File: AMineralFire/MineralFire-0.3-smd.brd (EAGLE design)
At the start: 109.9 x 77 mm, 86 parts, among them IC2 74LS09D, IC3 LM358D, Q1 20MHz, Q2 20MHz, Q3 MMBT3906LT1SMD, Q4 MMBT3906LT1SMD, Q5 MMBT3906LT1SMD, Q6 MMBT3906LT1SMD, Q7 MMBT3906LT1SMD, Q8 MMBT3906LT1SMD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

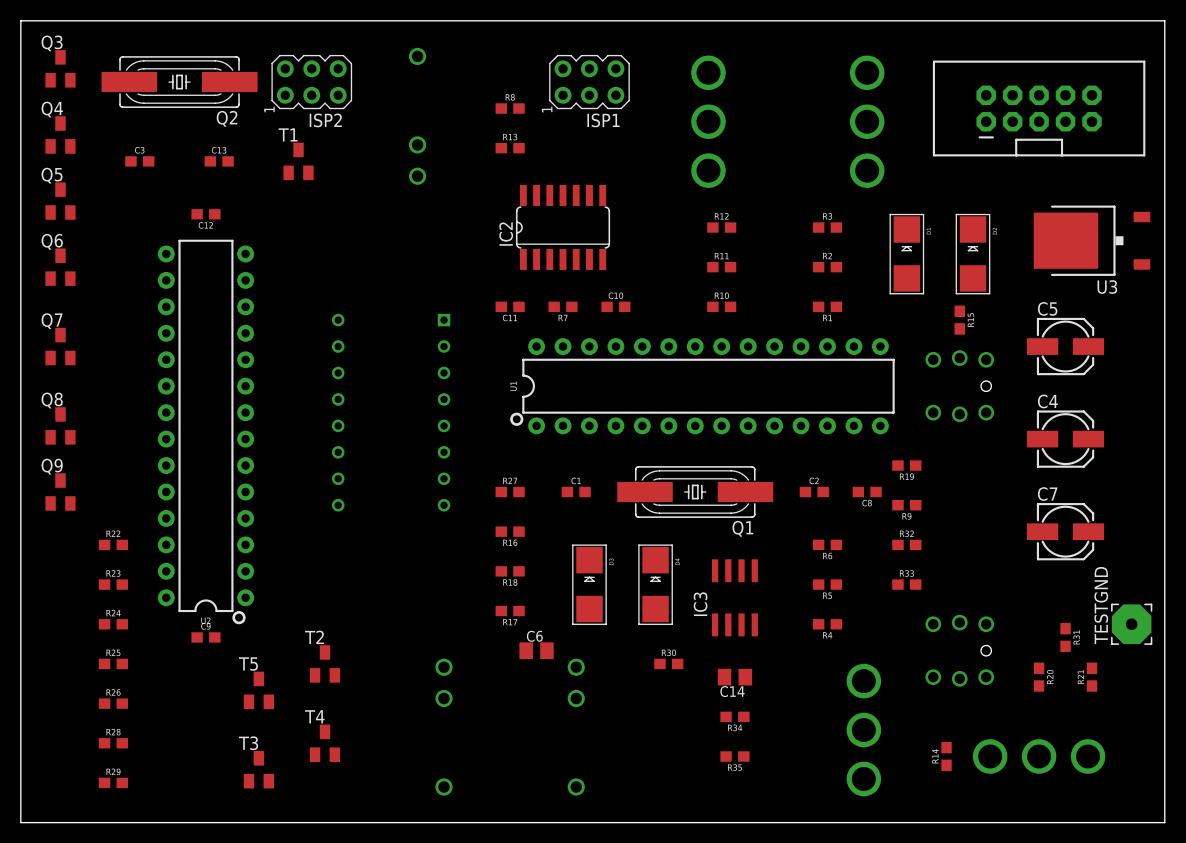
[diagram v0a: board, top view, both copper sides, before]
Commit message: 0.3-smd nor fully smd
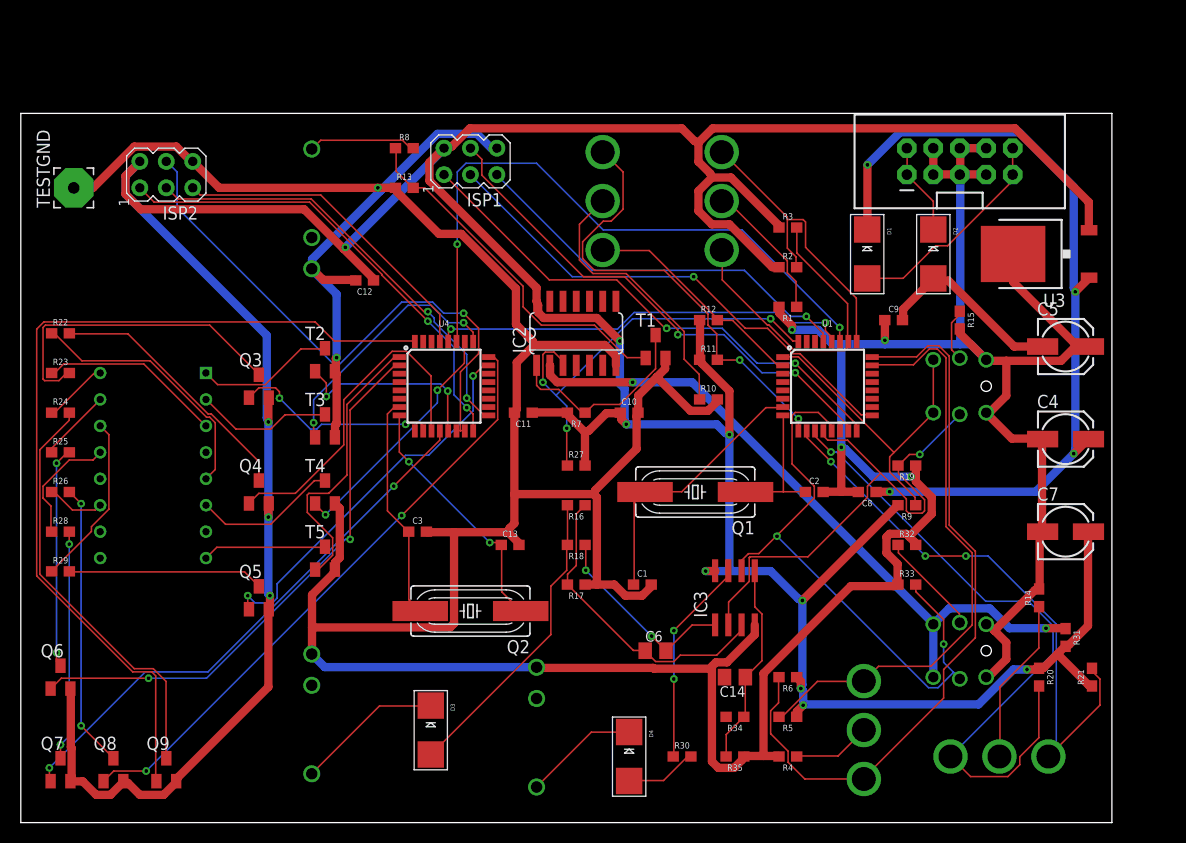
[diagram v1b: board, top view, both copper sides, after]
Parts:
- removed U2: 328P, SparkFun-IC-Microcontroller:DIP28
- added U4: ATMEGA328P_TQFP, SparkFun-IC-Microcontroller:TQFP32-08
- U1: value 328P -> ATMEGA328P_TQFP; device SparkFun-IC-Microcontroller:DIP28 -> SparkFun-IC-Microcontroller:TQFP32-08
- moved TESTGND 109.9 mm to (5.08, 61.0)
- moved C9 72.7 mm to (83.8, 48.3)
- moved Q2 58.0 mm to (43.2, 20.3)
- moved C13 46.2 mm to (47.0, 26.7)
- moved C3 44.5 mm to (38.1, 27.9)
- moved Q5 42.6 mm to (22.9, 21.6)
- moved Q7 40.6 mm to (3.81, 5.08)
- moved Q6 39.4 mm to (3.81, 14.0)
- moved Q4 39.2 mm to (22.9, 31.8)
- moved T1 38.6 mm to (61.0, 45.7)
- moved Q3 35.9 mm to (22.9, 41.9)
- moved T3 33.6 mm to (29.2, 38.1)
- moved Q8 33.4 mm to (8.89, 5.08)
- moved T2 29.2 mm to (29.2, 44.5)
- moved Q9 28.5 mm to (14.0, 5.08)
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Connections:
- net +5V: now also U1.18, U1.4, U4.18, U4.20, U4.4; no longer U1.21, U1.7, U2.20, U2.21, U2.7
- net BUTLED: now also U1.13; no longer U1.15
- net B_TRIG: now also U1.1; no longer U1.5
- net C-DIG1: now also U4.13; no longer U2.15
- net C-DIG2: now also U4.25; no longer U2.25
- net C-DIG3: now also U4.26; no longer U2.26
- net C-DIG4: now also U4.1; no longer U2.5
- net C-SEGA: now also U4.23; no longer U2.23
- net C-SEGB: now also U4.32; no longer U2.4
- net C-SEGC: now also U4.12; no longer U2.14
- net C-SEGD: now also U4.10; no longer U2.12
- net C-SEGDP: now also U4.9; no longer U2.11
- net C-SEGE: now also U4.11; no longer U2.13
- net C-SEGF: now also U4.24; no longer U2.24
- net C-SEGG: now also U4.2; no longer U2.6
- net CS: now also U1.14; no longer U1.16
- net GND: now also U1.3, U1.5, U4.21, U4.3, U4.5; no longer U1.22, U1.8, U2.22, U2.8
- net MISO: now also U1.16; no longer U1.18
- net MISO2: now also U4.16; no longer U2.18
- net MOSI: now also U1.15; no longer U1.17
- net MOSI2: now also U4.14, U4.15; no longer U2.16, U2.17
- net N$1: now also U1.7; no longer U1.9
- net N$2: now also U1.8; no longer U1.10
- net N$7: now also U4.7; no longer U2.9
- net N$8: now also U4.8; no longer U2.10
- net RST: now also U1.29; no longer U1.1
- net RST2: now also U4.29; no longer U2.1
- net SCK: now also U1.17; no longer U1.19
- net SCK2: now also U4.17; no longer U2.19
- net SCL: now also U4.28; no longer U2.28
- net SDA: now also U4.27; no longer U2.27
- net T1: now also U1.9; no longer U1.11
- net T2: now also U1.2; no longer U1.6
- net T7: now also U1.10; no longer U1.12
- net T8: now also U1.11; no longer U1.13
- net TRIG: now also U1.32; no longer U1.4
- net TRIGO: now also U1.12; no longer U1.14
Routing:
- net GND: track 0.00 -> 475.4 mm, vias 0 -> 6
- net +5V: track 0.00 -> 404.2 mm, vias 0 -> 12
- net C-SEGB: track 0.00 -> 86.6 mm
- net +12V: track 0.00 -> 79.6 mm, vias 0 -> 4
- net T6: track 0.00 -> 71.5 mm
- net LBUTTON: track 0.00 -> 66.9 mm, vias 0 -> 2
- net T8: track 0.00 -> 63.8 mm, vias 0 -> 1
- net SDA: track 0.00 -> 61.3 mm, vias 0 -> 2
- net C-SEGF: track 0.00 -> 58.9 mm, vias 0 -> 2
- net BUTLED: track 0.00 -> 58.7 mm, vias 0 -> 2
- net T5: track 0.00 -> 57.1 mm
- net T7: track 0.00 -> 55.9 mm, vias 0 -> 3
- net MOSI2: track 0.00 -> 55.0 mm, vias 0 -> 1
- net C-SEGG: track 0.00 -> 53.6 mm, vias 0 -> 2
- net C-SEGC: track 0.00 -> 52.7 mm, vias 0 -> 2
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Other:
- board size 109.9 x 77 mm -> 104.8 x 68.1 mm

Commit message: Added pull up resistors on I2C comms
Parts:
- added R36, R37: 4k7, SparkFun-Resistors:0603
- moved R10 23.4 mm to (48.3, 55.9)
- moved C1 15.9 mm to (73.7, 30.5)
- moved Q1 14.8 mm to (77.5, 24.1)
- moved C8 12.8 mm to (94.0, 33.0)
- moved R12 7.62 mm to (66.0, 40.6)
- moved IC3 7.41 mm to (62.2, 25.4)
- moved C2 5.24 mm to (81.3, 30.5)
- moved R32 5.24 mm to (90.2, 27.9)
- moved R33 5.24 mm to (90.2, 24.1)
- moved R11 3.81 mm to (66.0, 48.3)
- moved R19 2.84 mm to (87.6, 35.6)
- moved R9 2.84 mm to (87.6, 31.8)
- moved U1 1.27 mm to (76.2, 41.9)
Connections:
- net +5V: now also R36.1, R37.1
- net SCL: now also R37.2
- net SDA: now also R36.2
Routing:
- net C-SEGB: track 86.6 -> 54.4 mm, vias 0 -> 2
- net N$8: track 24.2 -> 40.1 mm
- net +12V: track 79.6 -> 63.6 mm, vias 4 -> 2
- net N$12: track 26.6 -> 11.1 mm
- net T7: track 55.9 -> 69.6 mm, vias 3 -> 1
- net SCK: track 48.2 -> 61.9 mm, vias 1 -> 0
- net GND: track 475.4 -> 461.9 mm, vias 6 -> 7
- net RST2: track 31.4 -> 43.8 mm
- net N$2: track 13.1 -> 25.2 mm, vias 0 -> 2
- net TRIGO: track 51.3 -> 63.1 mm, vias 1 -> 2
- net MOSI2: track 55.0 -> 43.7 mm
- net SDA: track 61.3 -> 50.1 mm, vias 2 -> 4
- net T6: track 71.5 -> 61.3 mm, vias 0 -> 2
- net T1: track 43.4 -> 34.5 mm, vias 2 -> 3
- net LBUTTON: track 66.9 -> 75.5 mm
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
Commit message: Layout chnaged
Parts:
- moved R35 30.7 mm to (64.8, 36.8)
- moved R34 24.2 mm to (67.3, 34.3)
- moved C14 21.7 mm to (61.0, 34.3)
- moved R14 19.3 mm to (80.0, 14.0)
- moved R4 14.8 mm to (66.0, 19.1)
- moved R20 10.2 mm to (87.6, 15.2)
- moved R21 10.2 mm to (92.7, 15.2)
- moved R33 9.16 mm to (82.5, 19.1)
- moved C6 8.98 mm to (52.1, 17.8)
- moved MODESW3 8.98 mm to (72.1, 7.62)
- moved R5 8.98 mm to (72.4, 19.1)
- moved Q2 7.73 mm to (41.9, 27.9)
- moved C13 7.73 mm to (48.3, 34.3)
- moved BUT1 7.62 mm to (90.2, 24.1)
- moved R6 6.35 mm to (77.5, 19.1)
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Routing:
- net +5V: track 400.2 -> 362.8 mm, vias 13 -> 15
- net T7: track 69.6 -> 49.6 mm, vias 1 -> 4
- net C-DIG3: track 32.0 -> 47.7 mm, vias 2 -> 0
- net MOSI2: track 43.7 -> 57.9 mm
- net T8: track 60.9 -> 46.9 mm, vias 1 -> 2
- net RST2: track 43.8 -> 30.8 mm
- net N$13: track 39.4 -> 51.7 mm
- net N$17: track 21.3 -> 32.5 mm, vias 2 -> 0
- net N$7: track 22.7 -> 12.8 mm
- net N$5: track 24.9 -> 34.1 mm
- net N$24: track 24.7 -> 16.2 mm, vias 2 -> 0
- net TRIG: track 47.1 -> 39.3 mm
- net N$8: track 40.1 -> 32.9 mm, vias 2 -> 0
- net TRIGO: track 63.1 -> 56.1 mm, vias 2 -> 1
- net N$2: track 25.2 -> 18.4 mm, vias 2 -> 0
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
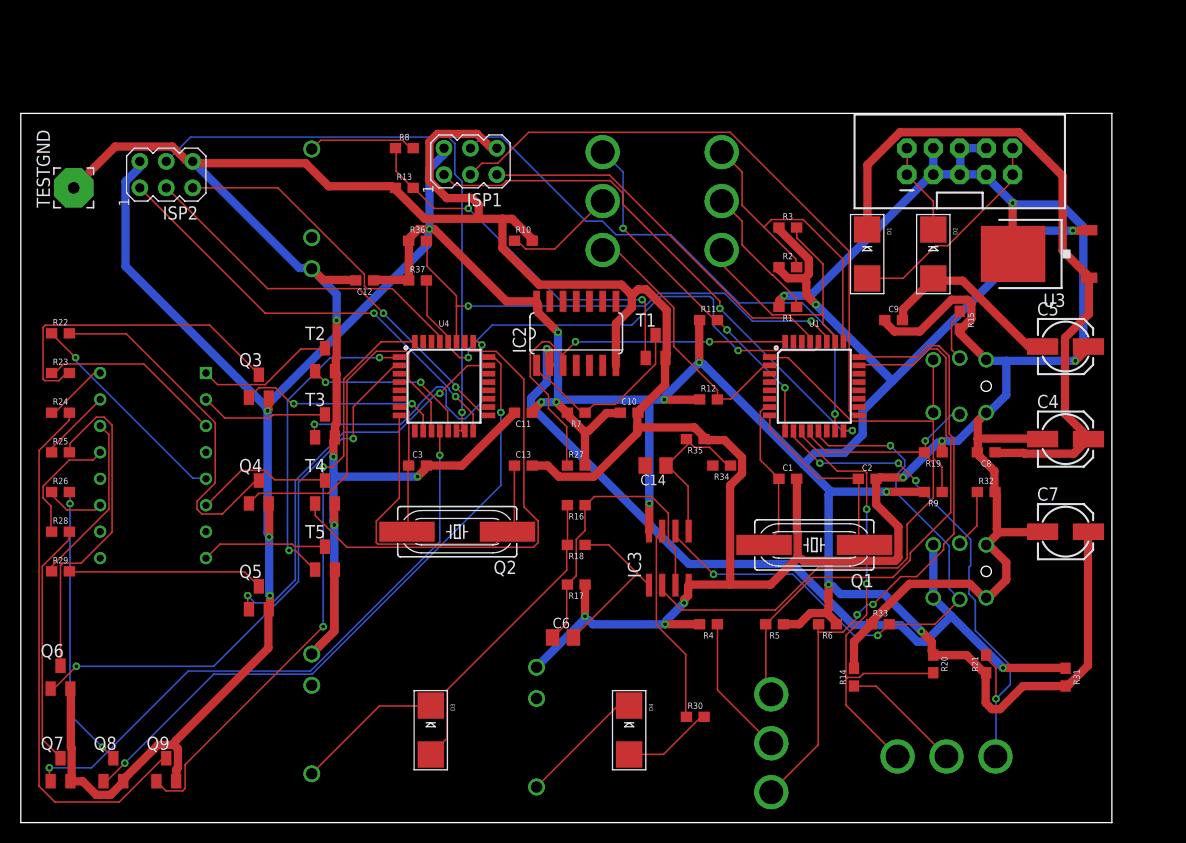
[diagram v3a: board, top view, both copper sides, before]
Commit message: taken boadr down to 100mm
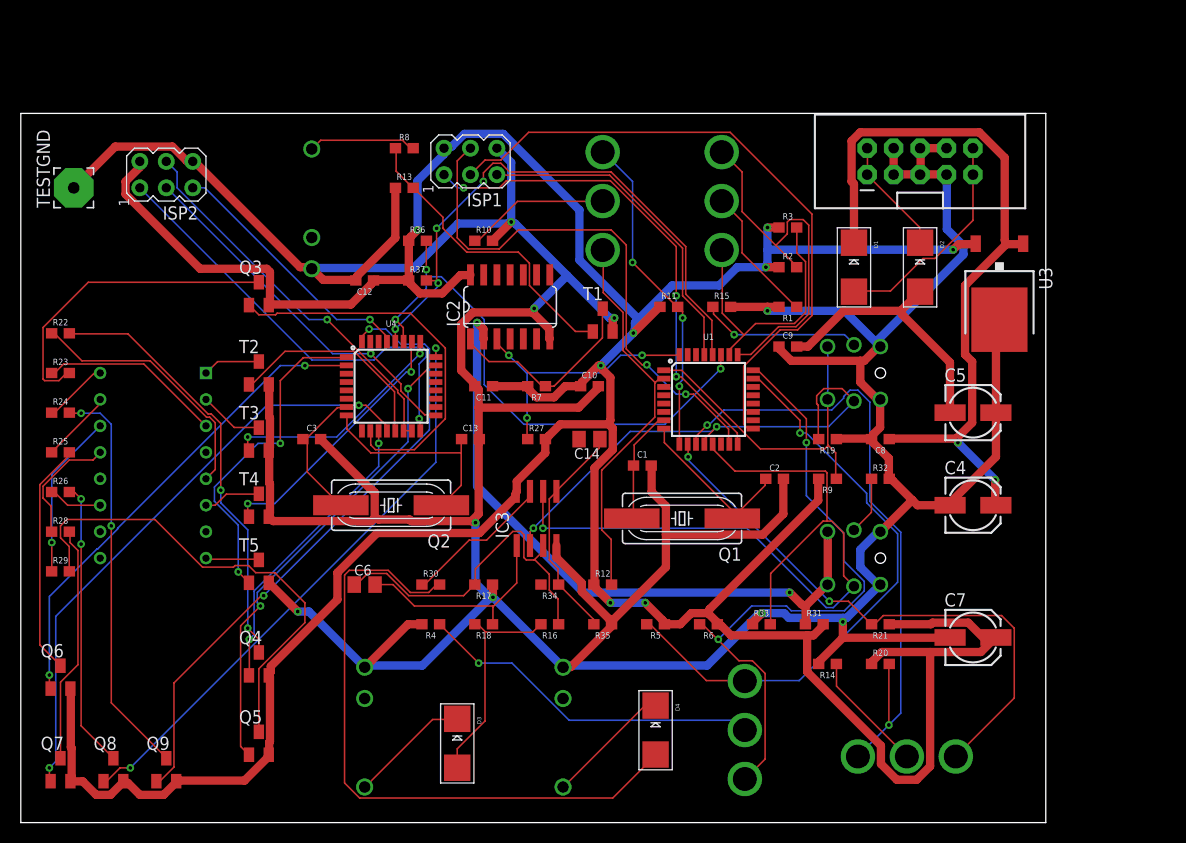
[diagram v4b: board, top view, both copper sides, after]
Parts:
- moved R30 28.4 mm to (39.4, 22.9)
- moved R4 26.7 mm to (39.4, 19.1)
- moved R31 24.7 mm to (76.2, 19.1), turned to 0 degrees
- moved R15 22.9 mm to (67.3, 49.5), turned to 0 degrees
- moved R12 20.5 mm to (55.9, 22.9)
- moved R34 20.1 mm to (50.8, 22.9)
- moved R35 19.9 mm to (55.9, 19.1)
- moved C6 19.7 mm to (33.0, 22.9)
- moved Q4 16.5 mm to (22.9, 15.2)
- moved C1 14.0 mm to (59.7, 34.3)
- moved Q5 14.0 mm to (22.9, 7.62)
- moved C7 13.5 mm to (91.4, 17.8)
- moved IC3 13.3 mm to (49.5, 29.2)
- moved Q1 13.0 mm to (63.5, 29.2)
- moved R18 11.7 mm to (44.5, 19.1)
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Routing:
- net N$22: track 8.70 -> 62.7 mm
- net N$20: track 18.8 -> 46.1 mm
- net C-DIG3: track 47.7 -> 25.2 mm, vias 0 -> 2
- net MOSI2: track 57.9 -> 37.2 mm
- net N$4: track 13.6 -> 33.5 mm, vias 0 -> 1
- net C-SEGD: track 19.7 -> 37.4 mm, vias 2 -> 0
- net T8: track 46.9 -> 62.7 mm
- net LBUTTON: track 79.2 -> 63.6 mm
- net BUTLED: track 59.1 -> 74.5 mm, vias 3 -> 1
- net TRIG: track 39.3 -> 26.2 mm, vias 2 -> 3
- net N$13: track 51.7 -> 38.7 mm, vias 0 -> 2
- net N$8: track 32.9 -> 20.4 mm
- net T2: track 26.1 -> 37.8 mm
- net N$31: track 5.15 -> 15.5 mm, vias 0 -> 1
- net N$17: track 32.5 -> 22.5 mm
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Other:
- board size 104.8 x 68.1 mm -> 98.4 x 68.1 mm
